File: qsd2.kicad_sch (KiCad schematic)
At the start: 64 parts, among them J1 5-1814832-1, J2 5-1814832-1, J3 Conn_02x08_Odd_Even, J4 SJ-3524-SMT, U1 SN74LVC1G14DBV, U10 GALI-39, U2 SN74LVC1G14DBV, U3 SN74CBT3253, U4 SN74AC74PW, U5 AD8226ARZ-R7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

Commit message: Gerbers done, ready to release V1.1.
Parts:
- added C7: 10uF, Capacitor_SMD:C_1206_3216Metric, symbol Device:C_Small
- C11: value 10uF -> 0.1uF
- R16: value 0 -> DNP
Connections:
- net 12V_FILT: now also C7.1; no longer C11.1
- net 12_0V: now also C11.1
- net GND: now also C7.2
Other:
- moved on the sheet: C11
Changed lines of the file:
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@@
   (junction (at 252.73 114.3) (diameter 0) (color 0 0 0 0)
   )
+  (junction (at 60.96 163.195) (diameter 0) (color 0 0 0 0)
+  )
   (junction (at 88.9 81.28) (diameter 0) (color 0 0 0 0)
   )
@@
     (stroke (width 0) (type default))
   )
+  (wire (pts (xy 53.34 163.195) (xy 60.96 163.195))
+    (stroke (width 0) (type default))
+  )
   (wire (pts (xy 137.16 83.82) (xy 137.16 86.36))
     (stroke (width 0) (type default))
@@
     (stroke (width 0) (type default))
   )
+  (wire (pts (xy 77.47 171.45) (xy 77.47 172.72))
+    (stroke (width 0) (type default))
+  )
   (wire (pts (xy 78.105 109.855) (xy 78.105 112.395))
     (stroke (width 0) (type default))
@@
     (stroke (width 0) (type default))
   )
-  (wire (pts (xy 53.34 163.195) (xy 65.405 163.195))
-    (stroke (width 0) (type default))
-  )
   (wire (pts (xy 139.7 171.45) (xy 139.7 172.72))
     (stroke (width 0) (type default))
@@
     (stroke (width 0) (type default))
   )
-  (wire (pts (xy 77.47 163.195) (xy 77.47 163.83))
+  (wire (pts (xy 77.47 163.195) (xy 77.47 166.37))
     (stroke (width 0) (type default))
   )
@@
     (stroke (width 0) (type default))
   )
+  (wire (pts (xy 60.96 163.195) (xy 65.405 163.195))
+    (stroke (width 0) (type default))
+  )
   (wire (pts (xy 226.695 106.68) (xy 226.695 108.585))
     (stroke (width 0) (type default))
@@
     (stroke (width 0) (type default))
   )
+  (wire (pts (xy 60.96 172.72) (xy 60.96 173.99))
+    (stroke (width 0) (type default))
+  )
   (wire (pts (xy 243.205 114.3) (xy 245.11 114.3))
     (stroke (width 0) (type default))
@@
     (stroke (width 0) (type default))
   )
+  (wire (pts (xy 60.96 163.195) (xy 60.96 167.64))
+    (stroke (width 0) (type default))
+  )
   (wire (pts (xy 121.92 96.52) (xy 128.27 96.52))
     (stroke (width 0) (type default))
@@
     (stroke (width 0) (type default))
   )
-  (wire (pts (xy 77.47 168.91) (xy 77.47 170.815))
-    (stroke (width 0) (type default))
-  )
   (wire (pts (xy 40.64 175.895) (xy 38.735 175.895))
     (stroke (width 0) (type default))
@@
     (stroke (width 0) (type default))
   )
-  (text "OR FERRITE BEAD" (at 58.039 166.878 0)
+  (text "OR FERRITE BEAD" (at 69.723 158.369 0)
     (effects (font (size 1.27 1.27)) (justify left bottom))
   )
@@
       (effects (font (size 1.27 1.27)))
     )
-    (property "Value" "0" (at 257.81 64.77 90)
+    (property "Value" "DNP" (at 257.81 64.77 90)
       (effects (font (size 1.27 1.27)))
     )
@@
     )
   )
+  (symbol (lib_id "power:GND") (at 77.47 172.72 0) (unit 1)
+    (in_bom yes) (on_board yes) (dnp no) (fields_autoplaced)
+    (property "Reference" "#PWR012" (at 77.47 179.07 0)
+      (effects (font (size 1.27 1.27)) hide)
+    )
+    (property "Value" "GND" (at 77.47 177.8 0)
+      (effects (font (size 1.27 1.27)))
+    )
+    (property "Footprint" "" (at 77.47 172.72 0)
+      (effects (font (size 1.27 1.27)) hide)
+    )
+    (property "Datasheet" "" (at 77.47 172.72 0)
+      (effects (font (size 1.27 1.27)) hide)
+    )
+    (pin "1")
+    (instances
+      (project "qsd2"
+        (path "/e85a7744-7948-44f7-b41f-dd9b75249984"
+          (reference "#PWR012") (unit 1)
+        )
+      )
+    )
+  )
   (symbol (lib_id "Device:R_Small_US") (at 55.245 93.98 0) (unit 1)
     (in_bom yes) (on_board yes) (dnp no) (fields_autoplaced)
@@
     )
   )
-  (symbol (lib_id "Device:C_Small") (at 77.47 166.37 0) (unit 1)
+  (symbol (lib_id "Device:C_Small") (at 60.96 170.18 0) (unit 1)
     (in_bom yes) (on_board yes) (dnp no) (fields_autoplaced)
-    (property "Reference" "C11" (at 80.01 165.1063 0)
+    (property "Reference" "C11" (at 64.516 168.9163 0)
       (effects (font (size 1.27 1.27)) (justify left))
     )
-    (property "Value" "10uF" (at 80.01 167.6463 0)
+    (property "Value" "0.1uF" (at 64.516 171.4563 0)
       (effects (font (size 1.27 1.27)) (justify left))
     )
-    (property "Footprint" "Capacitor_SMD:C_1206_3216Metric" (at 77.47 166.37 0)
+    (property "Footprint" "Capacitor_SMD:C_1206_3216Metric" (at 60.96 170.18 0)
       (effects (font (size 1.27 1.27)) hide)
     )
-    (property "Datasheet" "~" (at 77.47 166.37 0)
+    (property "Datasheet" "~" (at 60.96 170.18 0)
       (effects (font (size 1.27 1.27)) hide)
     )
@@
     )
   )
+  (symbol (lib_id "Device:C_Small") (at 77.47 168.91 0) (unit 1)
+    (in_bom yes) (on_board yes) (dnp no) (fields_autoplaced)
+    (property "Reference" "C7" (at 80.01 167.6463 0)
+      (effects (font (size 1.27 1.27)) (justify left))
+    )
+    (property "Value" "10uF" (at 80.01 170.1863 0)
+      (effects (font (size 1.27 1.27)) (justify left))
+    )
+    (property "Footprint" "Capacitor_SMD:C_1206_3216Metric" (at 77.47 168.91 0)
+      (effects (font (size 1.27 1.27)) hide)
+    )
+    (property "Datasheet" "~" (at 77.47 168.91 0)
+      (effects (font (size 1.27 1.27)) hide)
+    )
+    (pin "1")
+    (pin "2")
+    (instances
+      (project "qsd2"
+        (path "/e85a7744-7948-44f7-b41f-dd9b75249984"
+          (reference "C7") (unit 1)
+        )
+      )
+    )
+  )
   (symbol (lib_id "74xGxx:SN74LVC1G14DBV") (at 50.165 38.735 0) (unit 1)
     (in_bom yes) (on_board yes) (dnp no)
@@
     )
   )
-  (symbol (lib_id "power:GND") (at 77.47 170.815 0) (unit 1)
+  (symbol (lib_id "power:GND") (at 60.96 173.99 0) (unit 1)
     (in_bom yes) (on_board yes) (dnp no) (fields_autoplaced)
-    (property "Reference" "#PWR017" (at 77.47 177.165 0)
+    (property "Reference" "#PWR017" (at 60.96 180.34 0)
       (effects (font (size 1.27 1.27)) hide)
     )
-    (property "Value" "GND" (at 77.47 175.895 0)
+    (property "Value" "GND" (at 60.96 179.07 0)
       (effects (font (size 1.27 1.27)))
     )
-    (property "Footprint" "" (at 77.47 170.815 0)
+    (property "Footprint" "" (at 60.96 173.99 0)
       (effects (font (size 1.27 1.27)) hide)
     )
-    (property "Datasheet" "" (at 77.47 170.815 0)
+    (property "Datasheet" "" (at 60.96 173.99 0)
       (effects (font (size 1.27 1.27)) hide)
     )

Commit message: Ready to publish version 1.1.
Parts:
- C20, C21: value Not used -> DNP
- J1, J2: Description_1 (none) -> CONN SMA JACK STR 50 OHM PCB
- U5, U6: footprint AD8129ARZ:R_8_ADI -> 16TSOP:R_8_ADI
- U9: footprint DCY0004A_N -> 16TSOP:DCY0004A_N
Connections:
- no-connect marks 10 -> 9
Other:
- note added: "KF5N"
- moved on the sheet: C23, C26, C27, C6, U7, U8

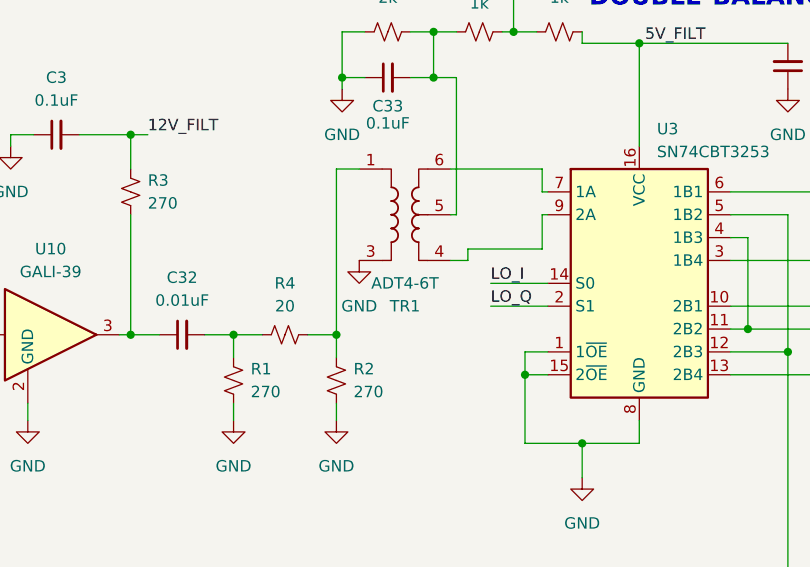
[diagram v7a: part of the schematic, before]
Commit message: Minor change to schematic part number.
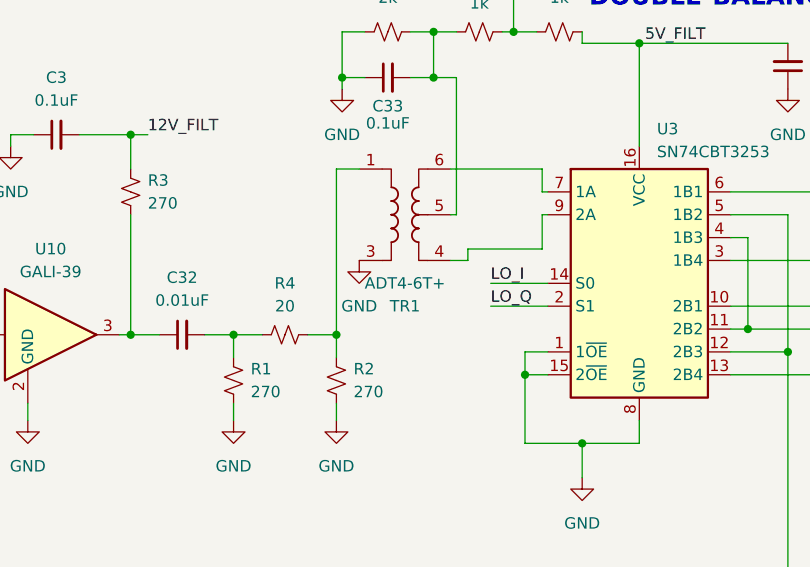
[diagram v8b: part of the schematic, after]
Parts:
- TR1: value ADT4-6T -> ADT4-6T+
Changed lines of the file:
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@@
 			)
 		)
-		(property "Value" "ADT4-6T"
+		(property "Value" "ADT4-6T+"
 			(at 85.725 104.14 0)
 			(effects
